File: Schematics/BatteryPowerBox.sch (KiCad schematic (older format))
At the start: 11 parts

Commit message: finalize schematic
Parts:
- U10: renamed from U?; symbol NAC3MPA-1-WOT:NAC3MPA-1-WOT -> BatteryBox-rescue:NAC3MPA-1-WOT-NAC3MPA-1-WOT
- gave numbers to parts that had none: 9
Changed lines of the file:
@@
 0V_OUT
 $Comp
-L Device:Battery BT?
+L Device:Battery BT2
 U 1 1 5F0C8690
 P 7150 3900
-F 0 "BT?" H 7258 3946 50  0000 L CNN
+F 0 "BT2" H 7258 3946 50  0000 L CNN
 F 1 "Battery" H 7258 3855 50  0000 L CNN
 F 2 "" V 7150 3960 50  0001 C CNN
@@
 $EndComp
 $Comp
-L Switch:SW_DPST_x2 SW?
-U 1 1 5F0CB6B3
+L Switch:SW_DPST_x2 SW2
+U 2 1 5F0CB6B3
 P 7150 3000
-F 0 "SW?" V 7196 2912 50  0000 R CNN
+F 0 "SW2" V 7196 2912 50  0000 R CNN
 F 1 "SW_DPST_x2" V 7105 2912 50  0000 R CNN
 F 2 "" H 7150 3000 50  0001 C CNN
 F 3 "~" H 7150 3000 50  0001 C CNN
-	1    7150 3000
+	2    7150 3000
 	0    -1   -1   0
 $EndComp
 $Comp
-L MyParts:F_Distributor U?
+L MyParts:F_Distributor U12
 U 1 1 5F0CCAE4
 P 4050 3550
-F 0 "U?" H 4050 2727 50  0000 C CNN
+F 0 "U12" H 4050 2727 50  0000 C CNN
 F 1 "F_Distributor" H 4050 2636 50  0000 C CNN
 F 2 "" H 4050 3550 50  0001 C CNN
@@
 $EndComp
 $Comp
-L MyParts:230V_KfzCharger U?
+L MyParts:230V_KfzCharger U11
 U 1 1 5F0CDA73
 P 3900 1100
-F 0 "U?" H 4100 1165 50  0000 C CNN
+F 0 "U11" H 4100 1165 50  0000 C CNN
 F 1 "230V_KfzCharger" H 4100 1074 50  0000 C CNN
 F 2 "" H 3900 1100 50  0001 C CNN
@@
 $EndComp
 $Comp
-L NAC3MPA-1-WOT:NAC3MPA-1-WOT U?
+L BatteryBox-rescue:NAC3MPA-1-WOT-NAC3MPA-1-WOT U10
 U 1 1 5F0CE699
 P 1250 5500
-F 0 "U?" H 1057 6267 50  0000 C CNN
+F 0 "U10" H 1057 6267 50  0000 C CNN
 F 1 "NAC3MPA-1-WOT" H 1057 6176 50  0000 C CNN
 F 2 "NAC3MPA-1-WOT" H 1250 5500 50  0001 L BNN
@@
 	2900 2050 3400 2050
 $Comp
-L Device:Fuse F?
+L Device:Fuse F3
 U 1 1 5F0D0D8A
 P 7150 2000
-F 0 "F?" H 7210 2046 50  0000 L CNN
+F 0 "F3" H 7210 2046 50  0000 L CNN
 F 1 "Fuse" H 7210 1955 50  0000 L CNN
 F 2 "" V 7080 2000 50  0001 C CNN
@@
 $EndComp
 $Comp
-L MyParts:Pulser U?
+L MyParts:Pulser U13
 U 1 1 5F0D362B
 P 6450 3650
-F 0 "U?" V 6404 3728 50  0000 L CNN
+F 0 "U13" V 6404 3728 50  0000 L CNN
 F 1 "Pulser" V 6495 3728 50  0000 L CNN
 F 2 "" H 6450 3650 50  0001 C CNN
@@
 	6350 1400 7150 1400
 $Comp
-L Connector:Conn_WallSocket J?
+L Connector:Conn_WallSocket J3
 U 1 1 5F0DCF32
 P 2150 6700
-F 0 "J?" H 2106 7025 50  0000 C CNN
+F 0 "J3" H 2106 7025 50  0000 C CNN
 F 1 "Conn_WallSocket" H 2106 6934 50  0000 C CNN
 F 2 "" H 1750 6700 50  0001 C CNN
@@
 $EndComp
 $Comp
-L Connector:Conn_WallSocket J?
+L Connector:Conn_WallSocket J4
 U 1 1 5F0DDC3E
 P 3300 6700
-F 0 "J?" H 3256 7025 50  0000 C CNN
+F 0 "J4" H 3256 7025 50  0000 C CNN
 F 1 "Conn_WallSocket" H 3256 6934 50  0000 C CNN
 F 2 "" H 2900 6700 50  0001 C CNN
@@
 $EndComp
 $Comp
-L Switch:SW_DPST_x2 SW?
+L Switch:SW_DPST_x2 SW2
 U 1 1 5F0DDE74
 P 5400 6300
-F 0 "SW?" V 5446 6212 50  0000 R CNN
+F 0 "SW2" V 5446 6212 50  0000 R CNN
 F 1 "SW_DPST_x2" V 5355 6212 50  0000 R CNN
 F 2 "" H 5400 6300 50  0001 C CNN
@@
 $EndComp
 $Comp
-L Device:Voltmeter_DC MES?
+L Device:Voltmeter_DC MES2
 U 1 1 5F0DE8B0
 P 4450 6650
-F 0 "MES?" H 4603 6696 50  0000 L CNN
+F 0 "MES2" H 4603 6696 50  0000 L CNN
 F 1 "Voltmeter_DC" H 4603 6605 50  0000 L CNN
 F 2 "" V 4450 6750 50  0001 C CNN

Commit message: some modifications
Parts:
- renumbered BT2 to BT1, F3 to F1, J3 to J1, J4 to J2, MES2 to MES1, SW2 to SW1, U10 to U1, U11 to U2, U12 to U3, U13 to U4
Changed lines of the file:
@@
 $Descr A4 11693 8268
 encoding utf-8
-Sheet 4 6
+Sheet 4 4
 Title ""
 Date ""
@@
 0V_OUT
 $Comp
-L Device:Battery BT2
+L Device:Battery BT1
 U 1 1 5F0C8690
 P 7150 3900
-F 0 "BT2" H 7258 3946 50  0000 L CNN
+F 0 "BT1" H 7258 3946 50  0000 L CNN
 F 1 "Battery" H 7258 3855 50  0000 L CNN
 F 2 "" V 7150 3960 50  0001 C CNN
@@
 $EndComp
 $Comp
-L Switch:SW_DPST_x2 SW2
+L Switch:SW_DPST_x2 SW1
 U 2 1 5F0CB6B3
 P 7150 3000
-F 0 "SW2" V 7196 2912 50  0000 R CNN
+F 0 "SW1" V 7196 2912 50  0000 R CNN
 F 1 "SW_DPST_x2" V 7105 2912 50  0000 R CNN
 F 2 "" H 7150 3000 50  0001 C CNN
@@
 $EndComp
 $Comp
-L MyParts:F_Distributor U12
+L MyParts:F_Distributor U3
 U 1 1 5F0CCAE4
 P 4050 3550
-F 0 "U12" H 4050 2727 50  0000 C CNN
+F 0 "U3" H 4050 2727 50  0000 C CNN
 F 1 "F_Distributor" H 4050 2636 50  0000 C CNN
 F 2 "" H 4050 3550 50  0001 C CNN
@@
 $EndComp
 $Comp
-L MyParts:230V_KfzCharger U11
+L MyParts:230V_KfzCharger U2
 U 1 1 5F0CDA73
 P 3900 1100
-F 0 "U11" H 4100 1165 50  0000 C CNN
+F 0 "U2" H 4100 1165 50  0000 C CNN
 F 1 "230V_KfzCharger" H 4100 1074 50  0000 C CNN
 F 2 "" H 3900 1100 50  0001 C CNN
@@
 $EndComp
 $Comp
-L BatteryBox-rescue:NAC3MPA-1-WOT-NAC3MPA-1-WOT U10
+L BatteryBox-rescue:NAC3MPA-1-WOT-NAC3MPA-1-WOT U1
 U 1 1 5F0CE699
 P 1250 5500
-F 0 "U10" H 1057 6267 50  0000 C CNN
+F 0 "U1" H 1057 6267 50  0000 C CNN
 F 1 "NAC3MPA-1-WOT" H 1057 6176 50  0000 C CNN
 F 2 "NAC3MPA-1-WOT" H 1250 5500 50  0001 L BNN
@@
 	2900 2050 3400 2050
 $Comp
-L Device:Fuse F3
+L Device:Fuse F1
 U 1 1 5F0D0D8A
 P 7150 2000
-F 0 "F3" H 7210 2046 50  0000 L CNN
+F 0 "F1" H 7210 2046 50  0000 L CNN
 F 1 "Fuse" H 7210 1955 50  0000 L CNN
 F 2 "" V 7080 2000 50  0001 C CNN
@@
 $EndComp
 $Comp
-L MyParts:Pulser U13
+L MyParts:Pulser U4
 U 1 1 5F0D362B
 P 6450 3650
-F 0 "U13" V 6404 3728 50  0000 L CNN
+F 0 "U4" V 6404 3728 50  0000 L CNN
 F 1 "Pulser" V 6495 3728 50  0000 L CNN
 F 2 "" H 6450 3650 50  0001 C CNN
@@
 	6350 1400 7150 1400
 $Comp
-L Connector:Conn_WallSocket J3
+L Connector:Conn_WallSocket J1
 U 1 1 5F0DCF32
 P 2150 6700
-F 0 "J3" H 2106 7025 50  0000 C CNN
+F 0 "J1" H 2106 7025 50  0000 C CNN
 F 1 "Conn_WallSocket" H 2106 6934 50  0000 C CNN
 F 2 "" H 1750 6700 50  0001 C CNN
@@
 $EndComp
 $Comp
-L Connector:Conn_WallSocket J4
+L Connector:Conn_WallSocket J2
 U 1 1 5F0DDC3E
 P 3300 6700
-F 0 "J4" H 3256 7025 50  0000 C CNN
+F 0 "J2" H 3256 7025 50  0000 C CNN
 F 1 "Conn_WallSocket" H 3256 6934 50  0000 C CNN
 F 2 "" H 2900 6700 50  0001 C CNN
@@
 $EndComp
 $Comp
-L Switch:SW_DPST_x2 SW2
+L Switch:SW_DPST_x2 SW1
 U 1 1 5F0DDE74
 P 5400 6300
-F 0 "SW2" V 5446 6212 50  0000 R CNN
+F 0 "SW1" V 5446 6212 50  0000 R CNN
 F 1 "SW_DPST_x2" V 5355 6212 50  0000 R CNN
 F 2 "" H 5400 6300 50  0001 C CNN
@@
 $EndComp
 $Comp
-L Device:Voltmeter_DC MES2
+L Device:Voltmeter_DC MES1
 U 1 1 5F0DE8B0
 P 4450 6650
-F 0 "MES2" H 4603 6696 50  0000 L CNN
+F 0 "MES1" H 4603 6696 50  0000 L CNN
 F 1 "Voltmeter_DC" H 4603 6605 50  0000 L CNN
 F 2 "" V 4450 6750 50  0001 C CNN

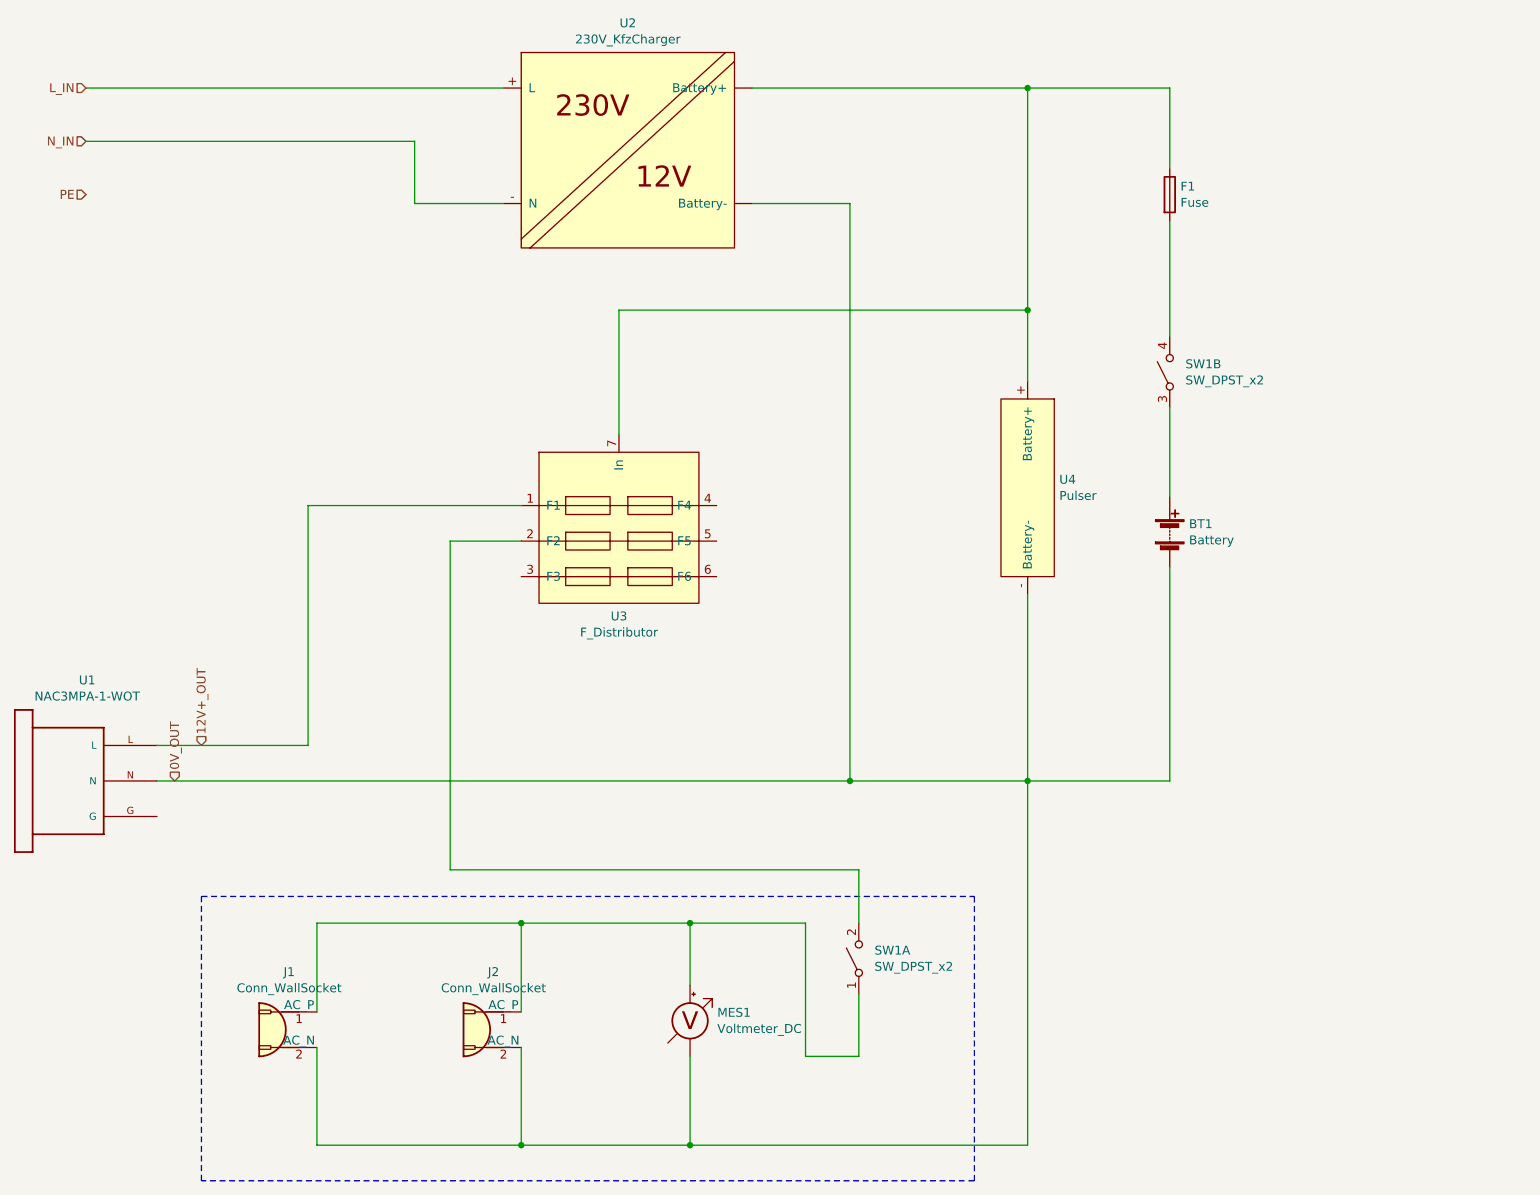
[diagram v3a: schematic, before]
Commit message: add terminal in Batterybox
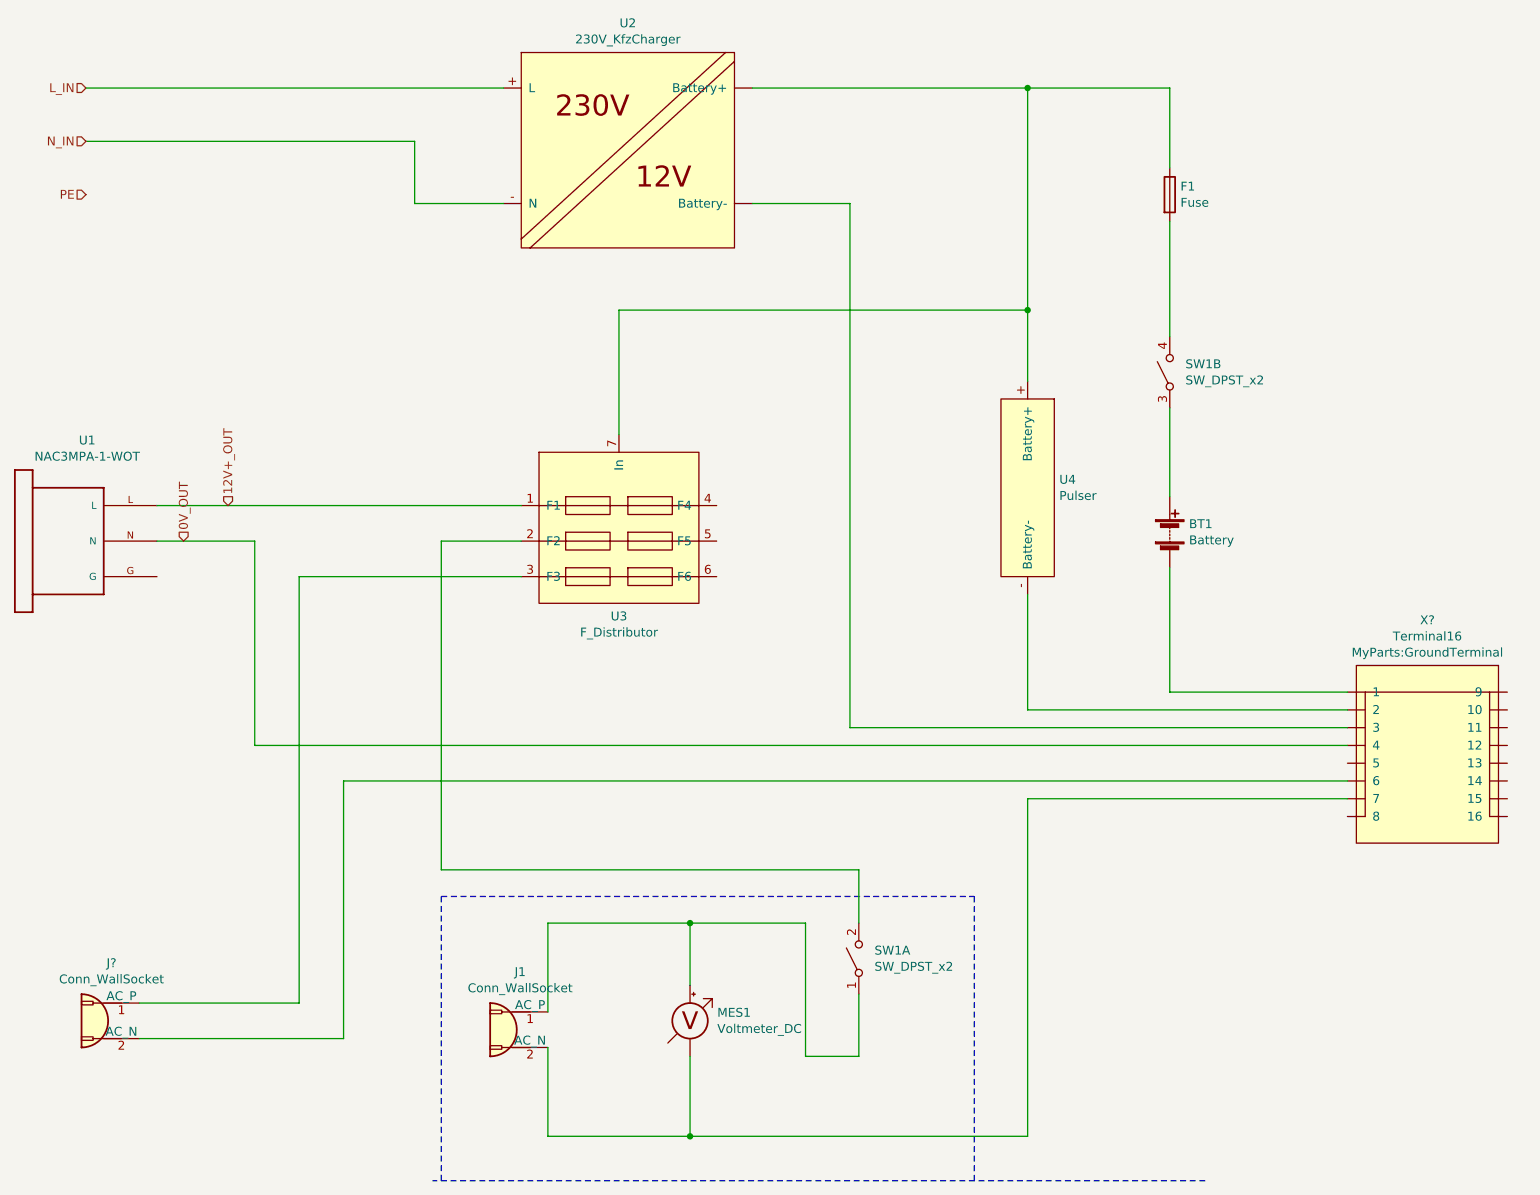
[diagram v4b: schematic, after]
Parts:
- removed J2: Conn_WallSocket, symbol Connector:Conn_WallSocket
- added J?: Conn_WallSocket, symbol Connector:Conn_WallSocket
- added X?: Terminal16, MyParts:GroundTerminal, symbol MyParts:Terminal16
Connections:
- net 0V_OUT: now also X?.~ (9); no longer BT1.2 (-), J1.2 (AC_N), MES1.1 (-), U2.~ (Battery-), U4.- (Battery-)
- net at U3.3 (F3): now also J?.1 (AC_P)
- new net: BT1.2 (-), X?.~ (9)
- new net: U2.~ (Battery-), X?.~ (9)
- new net: U4.- (Battery-), X?.~ (9)
- new net: J1.2 (AC_N), MES1.1 (-), X?.~ (9)
- new net: J?.2 (AC_N), X?.~ (9)
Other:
- moved on the sheet: J1, U1
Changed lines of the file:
@@
 $Descr A4 11693 8268
 encoding utf-8
-Sheet 4 4
+Sheet 2 4
 Title ""
 Date ""
@@
 Text HLabel 1050 1700 0    50   Input ~ 0
 N_IN
-Text HLabel 1700 5100 1    50   Input ~ 0
+Text HLabel 1850 3750 1    50   Input ~ 0
 12V+_OUT
-Text HLabel 1550 5300 1    50   Input ~ 0
+Text HLabel 1600 3950 1    50   Input ~ 0
 0V_OUT
 $Comp
@@
 L BatteryBox-rescue:NAC3MPA-1-WOT-NAC3MPA-1-WOT U1
 U 1 1 5F0CE699
-P 1250 5500
-F 0 "U1" H 1057 6267 50  0000 C CNN
-F 1 "NAC3MPA-1-WOT" H 1057 6176 50  0000 C CNN
-F 2 "NAC3MPA-1-WOT" H 1250 5500 50  0001 L BNN
-F 3 "" H 1250 5500 50  0001 C CNN
-	1    1250 5500
+P 1250 4150
+F 0 "U1" H 1057 4917 50  0000 C CNN
+F 1 "NAC3MPA-1-WOT" H 1057 4826 50  0000 C CNN
+F 2 "NAC3MPA-1-WOT" H 1250 4150 50  0001 L BNN
+F 3 "" H 1250 4150 50  0001 C CNN
+	1    1250 4150
 	1    0    0    -1
 $EndComp
@@
 	7150 2800 7150 2150
 Wire Wire Line
-	6350 4250 6350 5300
-Wire Wire Line
-	6350 5300 7150 5300
-Wire Wire Line
-	7150 5300 7150 4100
+	6350 4250 6350 4900
 Wire Wire Line
 	4050 3350 4050 2650
@@
 	4800 2050 5350 2050
 Wire Wire Line
-	5350 2050 5350 5300
-Wire Wire Line
-	5350 5300 6350 5300
-Connection ~ 6350 5300
-Connection ~ 5350 5300
-Wire Wire Line
-	1450 5300 5350 5300
-Wire Wire Line
-	2300 3750 3500 3750
-Wire Wire Line
-	1450 5100 2300 5100
-Wire Wire Line
-	2300 5100 2300 3750
+	5350 2050 5350 5000
 Text HLabel 1050 2000 0    50   Input ~ 0
 PE
@@
 L Connector:Conn_WallSocket J1
 U 1 1 5F0DCF32
-P 2150 6700
-F 0 "J1" H 2106 7025 50  0000 C CNN
-F 1 "Conn_WallSocket" H 2106 6934 50  0000 C CNN
-F 2 "" H 1750 6700 50  0001 C CNN
-F 3 "~" H 1750 6700 50  0001 C CNN
-	1    2150 6700
-	-1   0    0    -1
-$EndComp
-$Comp
-L Connector:Conn_WallSocket J2
-U 1 1 5F0DDC3E
-P 3300 6700
-F 0 "J2" H 3256 7025 50  0000 C CNN
-F 1 "Conn_WallSocket" H 3256 6934 50  0000 C CNN
-F 2 "" H 2900 6700 50  0001 C CNN
-F 3 "~" H 2900 6700 50  0001 C CNN
-	1    3300 6700
+P 3450 6700
+F 0 "J1" H 3406 7025 50  0000 C CNN
+F 1 "Conn_WallSocket" H 3406 6934 50  0000 C CNN
+F 2 "" H 3050 6700 50  0001 C CNN
+F 3 "~" H 3050 6700 50  0001 C CNN
+	1    3450 6700
 	-1   0    0    -1
 $EndComp
@@
 $EndComp
 Wire Wire Line
-	3500 3950 3100 3950
-Wire Wire Line
-	3100 3950 3100 5800
-Wire Wire Line
-	3100 5800 5400 5800
+	3500 3950 3050 3950
+Wire Wire Line
+	3050 3950 3050 5800
+Wire Wire Line
+	3050 5800 5400 5800
 Wire Wire Line
 	5400 5800 5400 6100
 Wire Wire Line
-	6350 7350 6350 5300
-Wire Wire Line
-	2350 7350 2350 6800
-Wire Wire Line
-	3500 6800 3500 7350
-Connection ~ 3500 7350
-Wire Wire Line
-	3500 7350 2350 7350
-Wire Wire Line
-	4450 6850 4450 7350
-Connection ~ 4450 7350
-Wire Wire Line
-	4450 7350 3500 7350
-Wire Wire Line
-	4450 7350 6350 7350
+	3650 7300 3650 6800
+Wire Wire Line
+	4450 6850 4450 7300
+Connection ~ 4450 7300
+Wire Wire Line
+	4450 7300 6350 7300
 Wire Wire Line
 	5100 6850 5100 6100
@@
 	5100 6100 4450 6100
 Wire Wire Line
-	2350 6100 2350 6600
-Wire Wire Line
-	3500 6600 3500 6100
-Connection ~ 3500 6100
-Wire Wire Line
-	3500 6100 2350 6100
+	3650 6100 3650 6600
 Wire Wire Line
 	4450 6450 4450 6100
 Connection ~ 4450 6100
 Wire Wire Line
-	4450 6100 3500 6100
-Wire Wire Line
 	5400 6500 5400 6850
 Wire Wire Line
 	5400 6850 5100 6850
 Wire Notes Line
-	1700 5950 6050 5950
+	3050 5950 6050 5950
 Wire Notes Line
 	6050 5950 6050 7550
 Wire Notes Line
-	6050 7550 1700 7550
-Wire Notes Line
-	1700 7550 1700 5950
+	7350 7550 3000 7550
+Wire Notes Line
+	3050 7550 3050 5950
+$Comp
+L MyParts:Terminal16 X?
+U 1 1 5F416C33
+P 8600 5250
+F 0 "X?" V 7745 5250 50  0000 C CNN
+F 1 "Terminal16" V 7836 5250 50  0000 C CNN
+F 2 "MyParts:GroundTerminal" V 7927 5250 50  0000 C CNN
+F 3 "" H 8650 5300 50  0001 C CNN
+	1    8600 5250
+	0    1    1    0
+$EndComp
+Wire Wire Line
+	8150 4800 7150 4800
+Wire Wire Line
+	7150 4800 7150 4100
+Wire Wire Line
+	8150 4900 6350 4900
+Wire Wire Line
+	8150 5400 6350 5400
+Wire Wire Line
+	6350 5400 6350 7300
+Wire Wire Line
+	8150 5000 5350 5000
+Wire Wire Line
+	3650 6100 4450 6100
+Wire Wire Line
+	3650 7300 4450 7300
+$Comp
+L Connector:Conn_WallSocket J?
+U 1 1 5F420731
+P 1150 6650
+F 0 "J?" H 1106 6975 50  0000 C CNN
+F 1 "Conn_WallSocket" H 1106 6884 50  0000 C CNN
+F 2 "" H 750 6650 50  0001 C CNN
+F 3 "~" H 750 6650 50  0001 C CNN
+	1    1150 6650
+	-1   0    0    -1
+$EndComp
+Wire Wire Line
+	3500 4150 2250 4150
+Wire Wire Line
+	2250 4150 2250 6550
+Wire Wire Line
+	2250 6550 1350 6550
+Wire Wire Line
+	1350 6750 2500 6750
+Wire Wire Line
+	2500 6750 2500 5300
+Wire Wire Line
+	1450 3750 3500 3750
+Wire Wire Line
+	8150 5300 2500 5300
+Wire Wire Line
+	8150 5100 2000 5100
+Wire Wire Line
+	2000 5100 2000 3950
+Wire Wire Line
+	2000 3950 1450 3950
 $EndSCHEMATC

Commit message: remove secon connector, switch with 230V land power
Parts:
- removed U4: Pulser, symbol MyParts:Pulser
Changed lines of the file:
@@
 	1    0    0    -1
-$EndComp
-$Comp
-L MyParts:Pulser U4
-U 1 1 5F0D362B
-P 6450 3650
-F 0 "U4" V 6404 3728 50  0000 L CNN
-F 1 "Pulser" V 6495 3728 50  0000 L CNN
-F 2 "" H 6450 3650 50  0001 C CNN
-F 3 "" H 6450 3650 50  0001 C CNN
-	1    6450 3650
-	0    1    1    0
 $EndComp
 Wire Wire Line
@@
 	7150 2800 7150 2150
 Wire Wire Line
-	6350 4250 6350 4900
-Wire Wire Line
 	4050 3350 4050 2650
 Wire Wire Line
 	4050 2650 6350 2650
-Connection ~ 6350 2650
-Wire Wire Line
-	6350 2650 6350 3050
 Wire Wire Line
 	4800 1400 6350 1400
@@
 	7150 4800 7150 4100
 Wire Wire Line
-	8150 4900 6350 4900
-Wire Wire Line
 	8150 5400 6350 5400

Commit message: modyfy schematic regarding new concept (still in work)
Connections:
- wire segments 44 -> 48
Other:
- moved on the sheet: F1, SW1B
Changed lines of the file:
@@
 L Switch:SW_DPST_x2 SW1
 U 2 1 5F0CB6B3
-P 7150 3000
-F 0 "SW1" V 7196 2912 50  0000 R CNN
-F 1 "SW_DPST_x2" V 7105 2912 50  0000 R CNN
-F 2 "" H 7150 3000 50  0001 C CNN
-F 3 "~" H 7150 3000 50  0001 C CNN
-	2    7150 3000
+P 7150 2000
+F 0 "SW1" V 7196 1912 50  0000 R CNN
+F 1 "SW_DPST_x2" V 7105 1912 50  0000 R CNN
+F 2 "" H 7150 2000 50  0001 C CNN
+F 3 "~" H 7150 2000 50  0001 C CNN
+	2    7150 2000
 	0    -1   -1   0
 $EndComp
@@
 Wire Wire Line
 	2900 2050 3400 2050
-$Comp
-L Device:Fuse F1
-U 1 1 5F0D0D8A
-P 7150 2000
-F 0 "F1" H 7210 2046 50  0000 L CNN
-F 1 "Fuse" H 7210 1955 50  0000 L CNN
-F 2 "" V 7080 2000 50  0001 C CNN
-F 3 "~" H 7150 2000 50  0001 C CNN
-	1    7150 2000
-	1    0    0    -1
-$EndComp
-Wire Wire Line
-	7150 3700 7150 3200
-Wire Wire Line
-	7150 2800 7150 2150
 Wire Wire Line
 	4050 3350 4050 2650
 Wire Wire Line
 	4050 2650 6350 2650
-Wire Wire Line
-	4800 1400 6350 1400
 Wire Wire Line
 	4800 2050 5350 2050
@@
 PE
 Wire Wire Line
-	7150 1400 7150 1850
-Wire Wire Line
 	6350 1400 6350 2650
-Connection ~ 6350 1400
 Wire Wire Line
 	6350 1400 7150 1400
@@
 Wire Wire Line
 	2000 3950 1450 3950
+Wire Wire Line
+	7150 1400 7150 1800
+Wire Wire Line
+	7150 2800 7150 2200
+$Comp
+L Device:Fuse F1
+U 1 1 5F0D0D8A
+P 7150 2950
+F 0 "F1" H 7210 2996 50  0000 L CNN
+F 1 "Fuse" H 7210 2905 50  0000 L CNN
+F 2 "" V 7080 2950 50  0001 C CNN
+F 3 "~" H 7150 2950 50  0001 C CNN
+	1    7150 2950
+	1    0    0    -1
+$EndComp
+Connection ~ 7150 2200
+Wire Wire Line
+	7150 2200 7150 2150
+Connection ~ 7150 1800
+Wire Wire Line
+	7150 1800 7150 1850
+Wire Wire Line
+	7150 3100 7150 3700
+Wire Wire Line
+	4600 3750 5000 3750
+Wire Wire Line
+	5000 3750 5000 1400
+Wire Wire Line
+	5000 1400 4800 1400
 $EndSCHEMATC
